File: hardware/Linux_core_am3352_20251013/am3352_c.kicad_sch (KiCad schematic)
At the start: 1 part, among them U1 AM3352BZCZ100

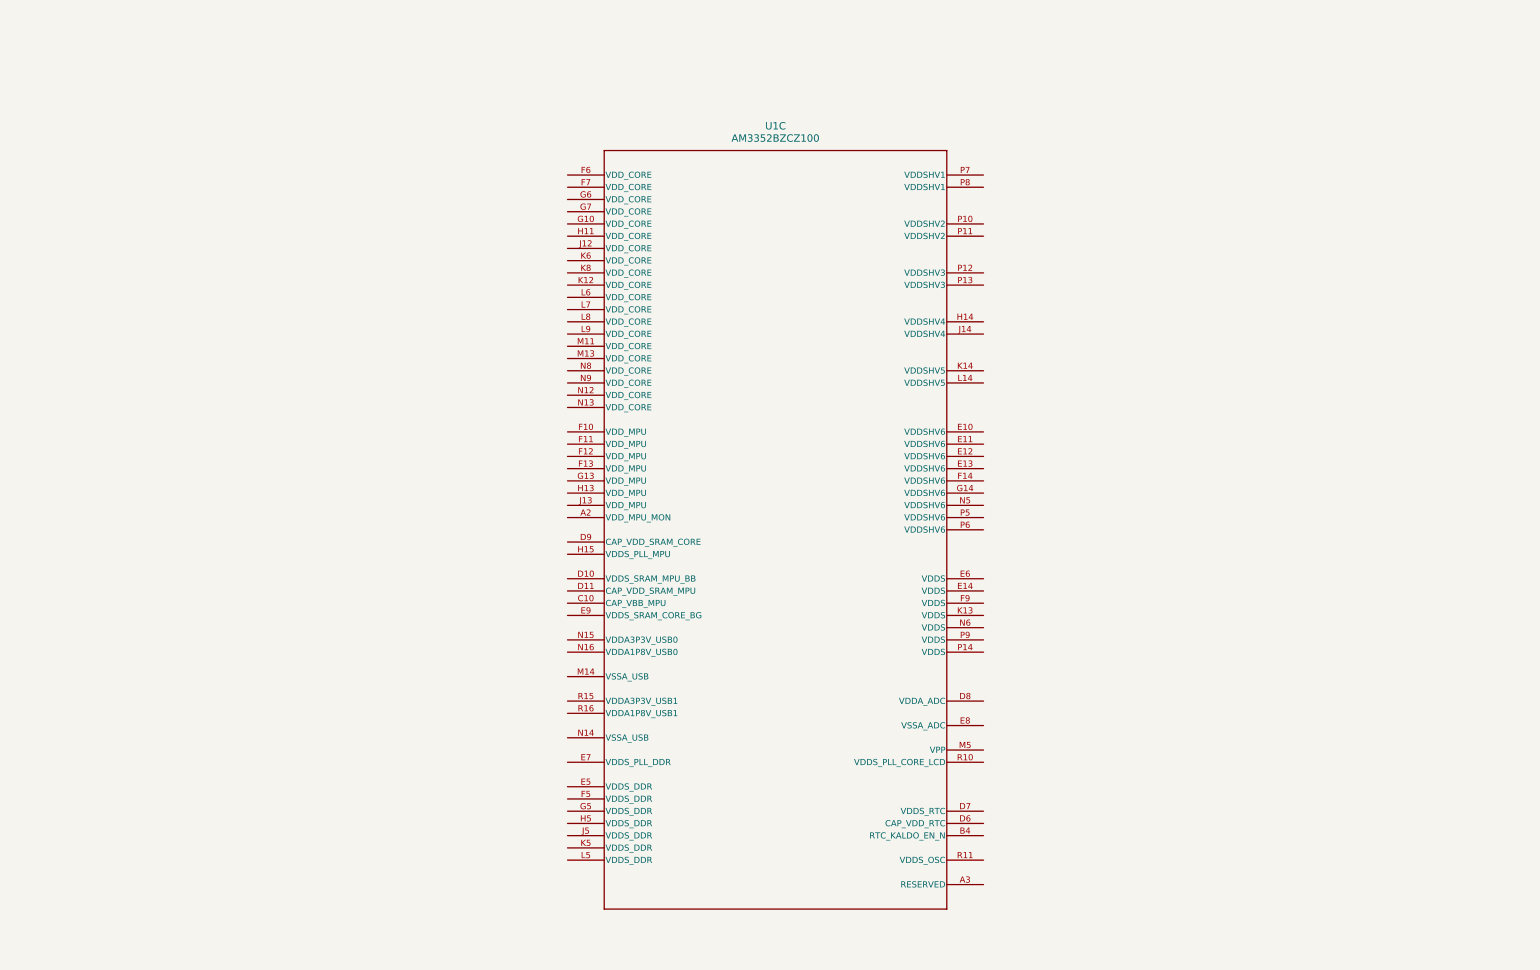
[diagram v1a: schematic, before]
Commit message: update schematic diagram
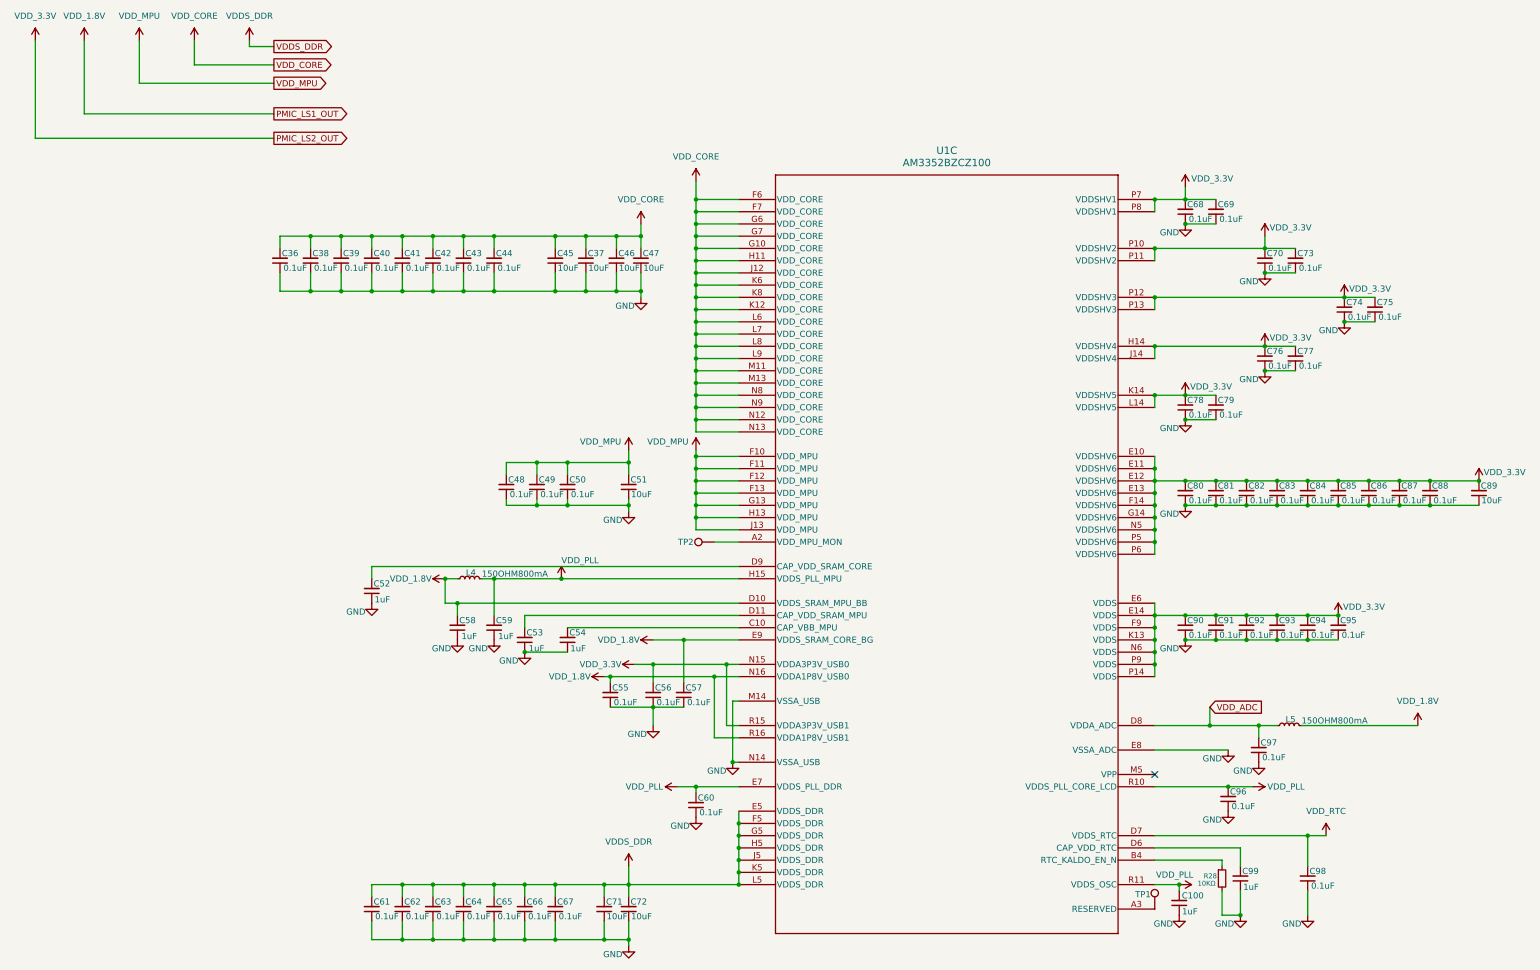
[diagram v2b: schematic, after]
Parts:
- added C100, C52, C53, C54, C58, C59, C99: 1uF, symbol Device:C_Small
- added C36, C38, C39, C40, C41, C42, C43, C44, C48, C49, C50, C55, C56, C57, C60, C61, C62, C63, C64, C65, C66, C67, C68, C69, C70, C73, C74, C75, C76, C77, C78, C79, C80, C81, C82, C83, C84, C85, C86, C87, C88, C90, C91, C92, C93, C94, C95, C96, C97, C98: 0.1uF, symbol Device:C_Small
- added C37, C45, C46, C47, C51, C71, C72, C89: 10uF, symbol Device:C_Small
- added L4, L5: 150OHM800mA, symbol Device:L_Small
- added R28: 10KΩ, symbol Device:R_Small
- added TP1, TP2: TestPoint, symbol Connector:TestPoint
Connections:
- net at U1.A2 (VDD_MPU_MON): now also TP2.1
- net at U1.A3 (RESERVED): now also TP1.1
- net at U1.B4 (RTC_KALDO_EN_N): now also R28.1
- net at U1.C10 (CAP_VBB_MPU): now also C54.2
- net VDD_1.8V: now reaches U1.D10 (VDDS_SRAM_MPU_BB)
- net VDD_1.8V: now also U1.E9 (VDDS_SRAM_CORE_BG), U1.N16 (VDDA1P8V_USB0), U1.R16 (VDDA1P8V_USB1), C55.2, C57.2, C58.2, L4.1, L5.2
- net at U1.D11 (CAP_VDD_SRAM_MPU): now also C53.2
- net at U1.D6 (CAP_VDD_RTC): now also C99.2
- net VDD_RTC: now reaches U1.D7 (VDDS_RTC)
- net VDD_RTC: now also C98.2
- net VDD_ADC: now reaches U1.D8 (VDDA_ADC)
- net VDD_ADC: now also C97.2, L5.1
- net at U1.D9 (CAP_VDD_SRAM_CORE): now also C52.2
- net VDD_3.3V: now reaches U1.E10 (VDDSHV6)
- net VDD_3.3V: now also U1.E11 (VDDSHV6), U1.E12 (VDDSHV6), U1.E13 (VDDSHV6), U1.E14 (VDDS), U1.E6 (VDDS), U1.F14 (VDDSHV6), U1.F9 (VDDS), U1.G14 (VDDSHV6), U1.H14 (VDDSHV4), U1.J14 (VDDSHV4), U1.K13 (VDDS), U1.K14 (VDDSHV5), U1.L14 (VDDSHV5), U1.N15 (VDDA3P3V_USB0), U1.N5 (VDDSHV6), U1.N6 (VDDS), U1.P10 (VDDSHV2), U1.P11 (VDDSHV2), U1.P12 (VDDSHV3), U1.P13 (VDDSHV3), U1.P14 (VDDS), U1.P5 (VDDSHV6), U1.P6 (VDDSHV6), U1.P7 (VDDSHV1), U1.P8 (VDDSHV1), U1.P9 (VDDS), U1.R15 (VDDA3P3V_USB1), C56.2, C68.2, C69.2, C70.2, C73.2, C74.2, C75.2, C76.2, C77.2, C78.2, C79.2, C80.2, C81.2, C82.2, C83.2, C84.2, C85.2, C86.2, C87.2, C88.2, C89.2, C90.2, C91.2, C92.2, C93.2, C94.2, C95.2
- net VDDS_DDR: now reaches U1.E5 (VDDS_DDR)
- net VDDS_DDR: now also U1.F5 (VDDS_DDR), U1.G5 (VDDS_DDR), U1.H5 (VDDS_DDR), U1.J5 (VDDS_DDR), U1.K5 (VDDS_DDR), U1.L5 (VDDS_DDR), C61.2, C62.2, C63.2, C64.2, C65.2, C66.2, C67.2, C71.2, C72.2
- net VDD_PLL: now reaches U1.E7 (VDDS_PLL_DDR)
- net VDD_PLL: now also U1.H15 (VDDS_PLL_MPU), U1.R10 (VDDS_PLL_CORE_LCD), U1.R11 (VDDS_OSC), C100.2, C59.2, C60.2, C96.2, L4.2
- net GND: now reaches U1.E8 (VSSA_ADC)
- net GND: now also U1.M14 (VSSA_USB), U1.N14 (VSSA_USB), C100.1, C36.1, C37.1, C38.1, C39.1, C40.1, C41.1, C42.1, C43.1, C44.1, C45.1, C46.1, C47.1, C48.1, C49.1, C50.1, C51.1, C52.1, C53.1, C54.1, C55.1, C56.1, C57.1, C58.1, C59.1, C60.1, C61.1, C62.1, C63.1, C64.1, C65.1, C66.1, C67.1, C68.1, C69.1, C70.1, C71.1, C72.1, C73.1, C74.1, C75.1, C76.1, C77.1, C78.1, C79.1, C80.1, C81.1, C82.1, C83.1, C84.1, C85.1, C86.1, C87.1, C88.1, C89.1, C90.1, C91.1, C92.1, C93.1, C94.1, C95.1, C96.1, C97.1, C98.1, C99.1, R28.2
- net VDD_MPU: now reaches U1.F10 (VDD_MPU)
- net VDD_MPU: now also U1.F11 (VDD_MPU), U1.F12 (VDD_MPU), U1.F13 (VDD_MPU), U1.G13 (VDD_MPU), U1.H13 (VDD_MPU), U1.J13 (VDD_MPU), C48.2, C49.2, C50.2, C51.2
- net VDD_CORE: now reaches U1.F6 (VDD_CORE)
- net VDD_CORE: now also U1.F7 (VDD_CORE), U1.G10 (VDD_CORE), U1.G6 (VDD_CORE), U1.G7 (VDD_CORE), U1.H11 (VDD_CORE), U1.J12 (VDD_CORE), U1.K12 (VDD_CORE), U1.K6 (VDD_CORE), U1.K8 (VDD_CORE), U1.L6 (VDD_CORE), U1.L7 (VDD_CORE), U1.L8 (VDD_CORE), U1.L9 (VDD_CORE), U1.M11 (VDD_CORE), U1.M13 (VDD_CORE), U1.N12 (VDD_CORE), U1.N13 (VDD_CORE), U1.N8 (VDD_CORE), U1.N9 (VDD_CORE), C36.2, C37.2, C38.2, C39.2, C40.2, C41.2, C42.2, C43.2, C44.2, C45.2, C46.2, C47.2
- no-connect marks 0 -> 1
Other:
- moved on the sheet: U1C
